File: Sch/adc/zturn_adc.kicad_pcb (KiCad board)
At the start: 4 copper layers, 90.5 x 80 mm, 117 parts, among them CN1 SMA, CN2 SMA, CN3 AudioJack, J1 JP4, J2 Header5, J3 JP2, J4 JP2, J5 JP2, J6 JP2, P1 CONN_02X40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

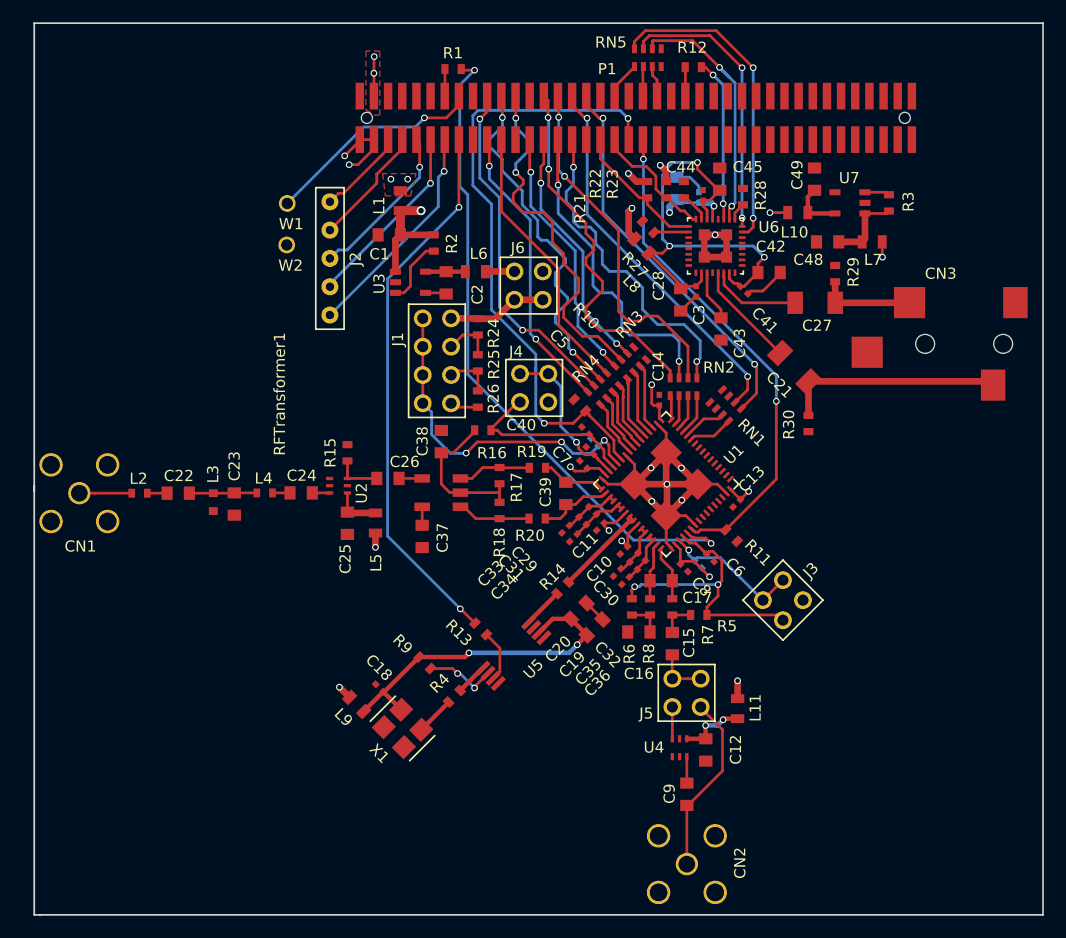
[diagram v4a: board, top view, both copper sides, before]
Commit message: moved jumper
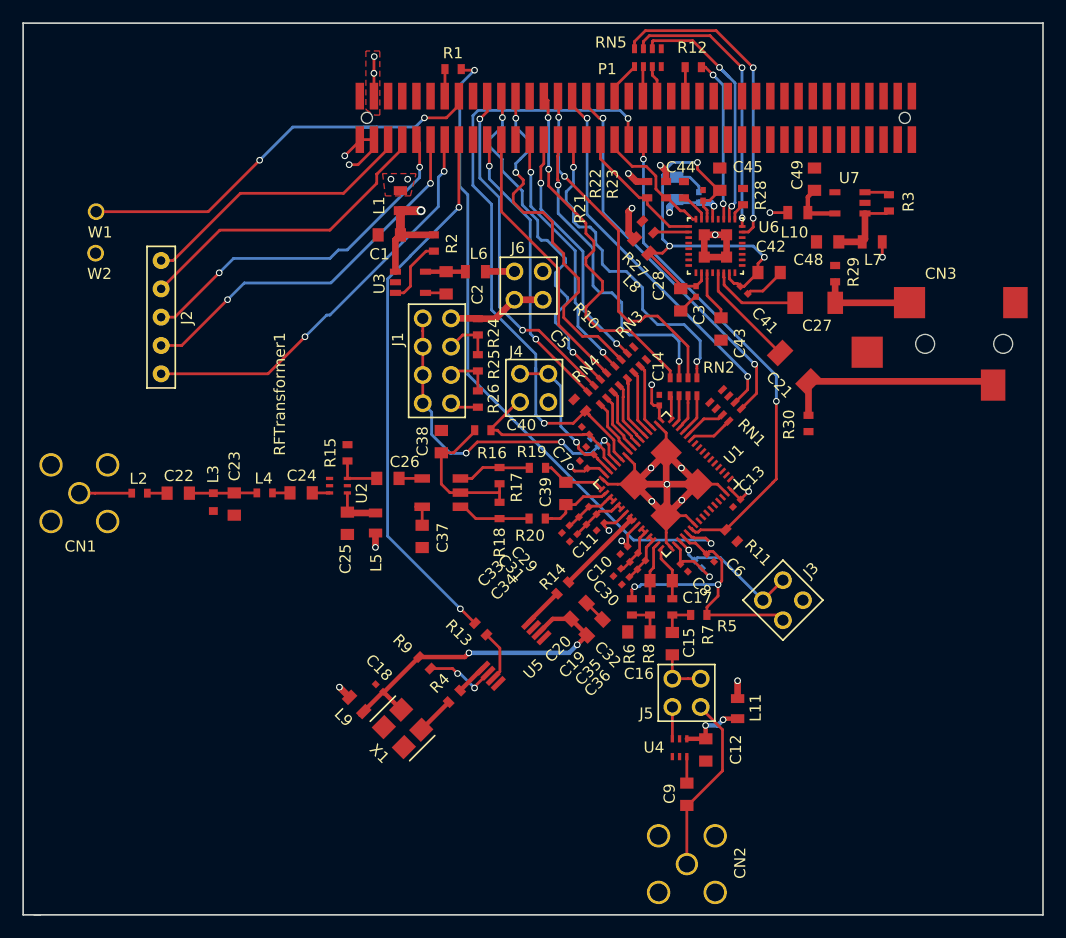
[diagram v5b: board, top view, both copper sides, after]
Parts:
- moved W1 17.2 mm to (92.5, 71.9)
- moved W2 17.2 mm to (92.5, 75.6)
- moved J2 16.0 mm to (98.4, 81.4)
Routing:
- net /CN/VDDIO_13_PL: track 20.7 -> 39.3 mm, vias 1 -> 2
- net /CN/JTAG_TMS: track 10.8 -> 28.1 mm
- net /CN/JTAG_TDI: track 14.6 -> 31.9 mm, vias 1 -> 2
- net /CN/JTAG_NRST: track 20.0 -> 37.3 mm, vias 1 -> 2
- net /CN/JTAG_TCK: track 8.01 -> 25.3 mm
- net /CN/JTAG_TDO: track 16.9 -> 34.1 mm, vias 1 -> 2
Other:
- board size 90.5 x 80 mm -> 91.5 x 80 mm
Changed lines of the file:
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@@
     (area 86.924999 47.3 188.35 135.075001)
     (thickness 1.6)
-    (drawings 8)
-    (tracks 970)
+    (drawings 7)
+    (tracks 991)
     (zones 0)
     (modules 117)
@@
   )
   (module adc_lib:M20-9990546 (layer F.Cu)
-    (at 113.525 76.11 270)
+    (at 98.38 81.38 270)
     (fp_text reference J2 (at 0.05 -2.305 270) (layer F.SilkS)
       (effects (font (size 1 1) (thickness 0.15)))
@@
   )
   (module adc_lib:68000-401HLF (layer F.Cu)
-    (at 109.7 71.175)
+    (at 92.55 71.915)
     (fp_text reference W1 (at 0.35 1.85) (layer F.SilkS)
       (effects (font (size 1 1) (thickness 0.15)))
@@
   )
   (module adc_lib:68000-401HLF (layer F.Cu)
-    (at 109.65 74.9)
+    (at 92.5 75.64)
     (fp_text reference W2 (at 0.35 1.85) (layer F.SilkS)
       (effects (font (size 1 1) (thickness 0.15)))
@@
     (arrow2b (pts (xy 180.5 55) (xy 181.086421 56.126504)))
   )
-  (dimension 89.5 (width 0.3) (layer Dwgs.User)
-    (gr_text "89.500 mm" (at 131.75 48.65) (layer Dwgs.User)
+  (dimension 91.440005 (width 0.3) (layer Dwgs.User)
+    (gr_text "91.440 mm" (at 131.741801 48.565 359.9812022) (layer Dwgs.User)
       (effects (font (size 1.5 1.5) (thickness 0.3)))
     )
-    (feature1 (pts (xy 176.5 54) (xy 176.5 47.3)))
-    (feature2 (pts (xy 87 54) (xy 87 47.3)))
-    (crossbar (pts (xy 87 50) (xy 176.5 50)))
-    (arrow1a (pts (xy 176.5 50) (xy 175.373496 50.586421)))
-    (arrow1b (pts (xy 176.5 50) (xy 175.373496 49.413579)))
-    (arrow2a (pts (xy 87 50) (xy 88.126504 50.586421)))
-    (arrow2b (pts (xy 87 50) (xy 88.126504 49.413579)))
+    (feature1 (pts (xy 177.46 54.07) (xy 177.462244 47.23)))
+    (feature2 (pts (xy 86.02 54.04) (xy 86.022244 47.2)))
+    (crossbar (pts (xy 86.021358 49.9) (xy 177.461358 49.93)))
+    (arrow1a (pts (xy 177.461358 49.93) (xy 176.334662 50.516051)))
+    (arrow1b (pts (xy 177.461358 49.93) (xy 176.335047 49.34321)))
+    (arrow2a (pts (xy 86.021358 49.9) (xy 87.147669 50.48679)))
+    (arrow2b (pts (xy 86.021358 49.9) (xy 87.148054 49.313949)))
   )
   (gr_line (start 87 135) (end 87.5 135) (layer Edge.Cuts) (width 0.15))
-  (gr_line (start 87 96.5) (end 87 135) (layer Edge.Cuts) (width 0.15))
-  (gr_line (start 177.5 135) (end 87.5 135) (layer Edge.Cuts) (width 0.15))
+  (gr_line (start 177.5 135) (end 86 135) (layer Edge.Cuts) (width 0.15))
   (gr_line (start 177.5 55) (end 177.5 135) (layer Edge.Cuts) (width 0.15))
-  (gr_line (start 87 55) (end 177.5 55) (layer Edge.Cuts) (width 0.15))
-  (gr_line (start 87 97) (end 87 55) (layer Edge.Cuts) (width 0.15))
+  (gr_line (start 86 55) (end 177.5 55) (layer Edge.Cuts) (width 0.15))
+  (gr_line (start 86 55) (end 86 135) (layer Edge.Cuts) (width 0.15))
   (segment (start 119.85 71.825) (end 119.85 74) (width 0.8) (layer F.Cu) (net 1))
   (segment (start 119.85 71.825) (end 121.7 71.825) (width 0.8) (layer F.Cu) (net 1))
@@
   (segment (start 126.797898 86.20742) (end 126.797899 86.207421) (width 0.25) (layer F.Cu) (net 40))
   (segment (start 126.797899 86.207421) (end 126.797899 87.997422) (width 0.25) (layer F.Cu) (net 40))
-  (segment (start 113.525 71.03) (end 114.286999 70.268001) (width 0.25) (layer F.Cu) (net 41))
-  (segment (start 114.286999 70.268001) (end 114.746999 70.268001) (width 0.25) (layer F.Cu) (net 41))
+  (segment (start 98.38 76.3) (end 99.45763 76.3) (width 0.25) (layer F.Cu) (net 41))
+  (segment (start 99.45763 76.3) (end 105.489629 70.268001) (width 0.25) (layer F.Cu) (net 41))
+  (segment (start 105.489629 70.268001) (end 114.746999 70.268001) (width 0.25) (layer F.Cu) (net 41))
   (segment (start 114.746999 70.268001) (end 118.745 66.27) (width 0.25) (layer F.Cu) (net 41))
   (segment (start 118.745 66.27) (end 118.745 65.45) (width 0.25) (layer F.Cu) (net 41))
+  (segment (start 98.38 78.84) (end 103.65 73.57) (width 0.25) (layer F.Cu) (net 42))
+  (segment (start 103.65 73.57) (end 113.525 73.57) (width 0.25) (layer F.Cu) (net 42))
   (segment (start 113.525 73.57) (end 117.725 69.37) (width 0.25) (layer F.Cu) (net 42))
   (segment (start 117.725 69.37) (end 117.725 68.55) (width 0.25) (layer F.Cu) (net 42))
@@
   (segment (start 117.735 68.55) (end 120.015 66.27) (width 0.25) (layer F.Cu) (net 42))
   (segment (start 120.015 66.27) (end 120.015 65.45) (width 0.25) (layer F.Cu) (net 42))
+  (segment (start 103.59 77.4) (end 104.88 76.11) (width 0.25) (layer B.Cu) (net 43))
+  (segment (start 104.88 76.11) (end 113.525 76.11) (width 0.25) (layer B.Cu) (net 43))
+  (segment (start 98.38 81.38) (end 99.61 81.38) (width 0.25) (layer F.Cu) (net 43))
+  (segment (start 99.61 81.38) (end 103.59 77.4) (width 0.25) (layer F.Cu) (net 43))
+  (via (at 103.59 77.4) (size 0.6) (drill 0.4) (layers F.Cu B.Cu) (net 43))
   (segment (start 121.575 67.925) (end 121.575 65.74) (width 0.25) (layer F.Cu) (net 43))
   (segment (start 121.575 65.74) (end 121.285 65.45) (width 0.25) (layer F.Cu) (net 43))
@@
   (segment (start 121.575 68.850002) (end 121.575 67.925) (width 0.25) (layer B.Cu) (net 43))
   (via (at 121.575 67.925) (size 0.6) (drill 0.4) (layers F.Cu B.Cu) (net 43))
-  (segment (start 122.55 69.375) (end 113.525 78.4) (width 0.25) (layer B.Cu) (net 44))
-  (segment (start 113.525 78.4) (end 113.525 78.65) (width 0.25) (layer B.Cu) (net 44))
+  (segment (start 122.55 69.375) (end 113.615 78.31) (width 0.25) (layer B.Cu) (net 44))
+  (segment (start 104.34 79.81) (end 105.84 78.31) (width 0.25) (layer B.Cu) (net 44))
+  (segment (start 105.84 78.31) (end 113.615 78.31) (width 0.25) (layer B.Cu) (net 44))
+  (segment (start 98.38 83.92) (end 100.23 83.92) (width 0.25) (layer F.Cu) (net 44))
+  (segment (start 100.23 83.92) (end 104.34 79.81) (width 0.25) (layer F.Cu) (net 44))
+  (via (at 104.34 79.81) (size 0.6) (drill 0.4) (layers F.Cu B.Cu) (net 44))
   (segment (start 122.555 65.45) (end 122.555 69.37) (width 0.25) (layer F.Cu) (net 44))
   (segment (start 122.555 69.37) (end 122.55 69.375) (width 0.25) (layer F.Cu) (net 44))
   (via (at 122.55 69.375) (size 0.6) (drill 0.4) (layers F.Cu B.Cu) (net 44))
+  (segment (start 111.29 83.14) (end 113.24 81.19) (width 0.25) (layer B.Cu) (net 45))
+  (segment (start 113.24 81.19) (end 113.525 81.19) (width 0.25) (layer B.Cu) (net 45))
+  (segment (start 98.38 86.46) (end 107.97 86.46) (width 0.25) (layer F.Cu) (net 45))
+  (segment (start 107.97 86.46) (end 111.29 83.14) (width 0.25) (layer F.Cu) (net 45))
+  (via (at 111.29 83.14) (size 0.6) (drill 0.4) (layers F.Cu B.Cu) (net 45))
   (segment (start 123.775 68.3) (end 123.775 65.5) (width 0.25) (layer F.Cu) (net 45))
   (segment (start 123.775 65.5) (end 123.825 65.45) (width 0.25) (layer F.Cu) (net 45))
@@
   (segment (start 123.845 61.53) (end 123.825 61.55) (width 0.25) (layer F.Cu) (net 54))
   (segment (start 123.825 61.55) (end 123.825 60.545) (width 0.25) (layer F.Cu) (net 54))
+  (segment (start 121.174999 64.325001) (end 117.75 64.325001) (width 0.25) (layer B.Cu) (net 55))
+  (segment (start 117.75 64.325001) (end 116.549999 64.325001) (width 0.25) (layer B.Cu) (net 55))
+  (segment (start 107.22 67.3) (end 110.194999 64.325001) (width 0.25) (layer B.Cu) (net 55))
+  (segment (start 110.194999 64.325001) (end 117.75 64.325001) (width 0.25) (layer B.Cu) (net 55))
+  (segment (start 92.55 71.915) (end 102.605 71.915) (width 0.25) (layer F.Cu) (net 55))
+  (segment (start 102.605 71.915) (end 107.22 67.3) (width 0.25) (layer F.Cu) (net 55))
+  (via (at 107.22 67.3) (size 0.6) (drill 0.4) (layers F.Cu B.Cu) (net 55))
   (segment (start 122 63.5) (end 121.174999 64.325001) (width 0.25) (layer B.Cu) (net 55))
-  (segment (start 121.174999 64.325001) (end 116.549999 64.325001) (width 0.25) (layer B.Cu) (net 55))
-  (segment (start 116.549999 64.325001) (end 110.449999 70.425001) (width 0.25) (layer B.Cu) (net 55))
-  (segment (start 110.449999 70.425001) (end 109.7 71.175) (width 0.25) (layer B.Cu) (net 55))
   (segment (start 125.095 61.55) (end 125.095 62.37) (width 0.25) (layer F.Cu) (net 55))
   (segment (start 123.965 63.5) (end 122 63.5) (width 0.25) (layer F.Cu) (net 55))

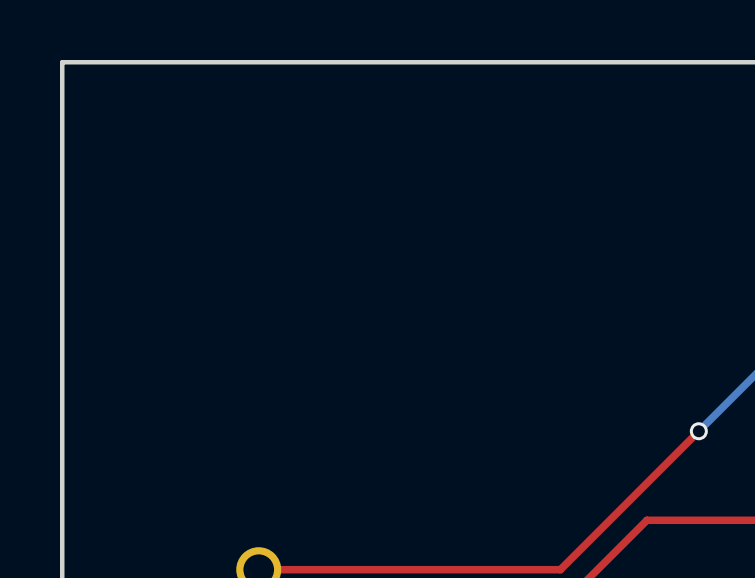
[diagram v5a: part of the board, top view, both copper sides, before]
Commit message: Add mounting hole
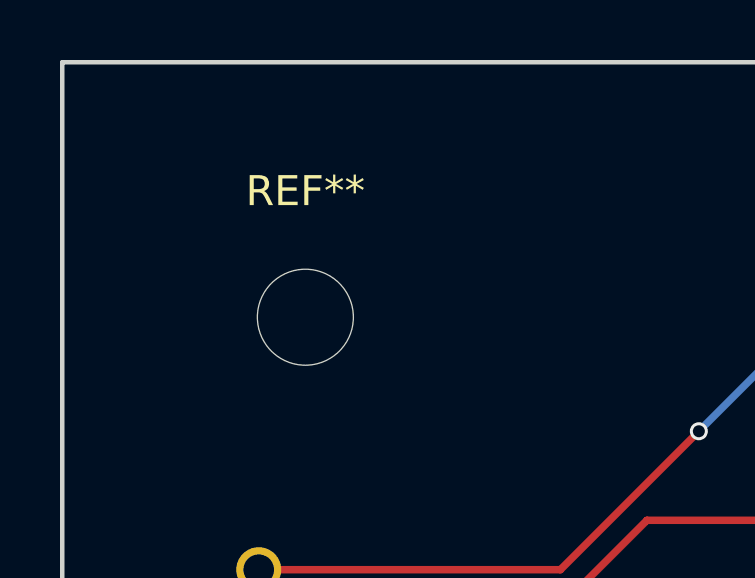
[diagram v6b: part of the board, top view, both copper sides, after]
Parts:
- added REF**: MountingHole_3.2mm_M3, Mounting_Holes:MountingHole_3.2mm_M3, F.Cu at (94.1, 63.5)
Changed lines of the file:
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@@
 (kicad_pcb (version 4) (host pcbnew 4.0.5)
   (general
-    (links 301)
+    (links 0)
     (no_connects 66)
-    (area 86.924999 47.3 188.35 135.075001)
+    (area 84.852381 47.2 188.35 135.075001)
     (thickness 1.6)
     (drawings 7)
     (tracks 991)
     (zones 0)
-    (modules 117)
+    (modules 118)
     (nets 189)
   )
@@
     (mod_text_size 1 1)
     (mod_text_width 0.15)
-    (pad_size 0.6 0.6)
-    (pad_drill 0.3)
+    (pad_size 3.2 3.2)
+    (pad_drill 3.2)
     (pad_to_mask_clearance 0.2)
     (aux_axis_origin 0 0)
@@
       (net 2 GND))
   )
+  (module Mounting_Holes:MountingHole_3.2mm_M3 (layer F.Cu)
+    (at 94.104 63.499)
+    (descr "Mounting Hole 3.2mm, no annular, M3")
+    (tags "mounting hole 3.2mm no annular m3")
+    (fp_text reference REF** (at 0 -4.2) (layer F.SilkS)
+      (effects (font (size 1 1) (thickness 0.15)))
+    )
+    (fp_text value MountingHole_3.2mm_M3 (at 0 4.2) (layer F.Fab)
+      (effects (font (size 1 1) (thickness 0.15)))
+    )
+    (fp_circle (center 0 0) (end 3.2 0) (layer Cmts.User) (width 0.15))
+    (fp_circle (center 0 0) (end 3.45 0) (layer F.CrtYd) (width 0.05))
+    (pad 1 np_thru_hole circle (at 0 0) (size 3.2 3.2) (drill 3.2) (layers *.Cu *.Mask))
+  )
   (dimension 80 (width 0.3) (layer Dwgs.User)

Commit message: Add pour GND
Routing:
- net (no net): track 0.00 -> 11.7 mm, vias 0 -> 1
- net GND: track 76.1 -> 70.1 mm, vias 8 -> 6
- added copper zone on B.Cu, net GND
- added copper zone on F.Cu, net GND
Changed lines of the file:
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@@
 (kicad_pcb (version 4) (host pcbnew 4.0.5)
   (general
-    (links 0)
-    (no_connects 66)
-    (area 84.852381 47.2 188.35 135.075001)
+    (links 301)
+    (no_connects 35)
+    (area 84.546857 47.2 188.35 135.075001)
     (thickness 1.6)
     (drawings 7)
-    (tracks 991)
+    (tracks 989)
     (zones 0)
     (modules 118)
@@
     (1 In1.Cu power hide)
     (2 In2.Cu power hide)
-    (31 B.Cu signal)
+    (31 B.Cu signal hide)
     (32 B.Adhes user)
     (33 F.Adhes user)
@@
     (last_trace_width 0.25)
     (trace_clearance 0.2)
-    (zone_clearance 0.2)
+    (zone_clearance 0.6)
     (zone_45_only no)
     (trace_min 0.2)
@@
   (gr_line (start 86 55) (end 177.5 55) (layer Edge.Cuts) (width 0.15))
   (gr_line (start 86 55) (end 86 135) (layer Edge.Cuts) (width 0.15))
+  (segment (start 117.37 79.23) (end 117.37 77.98141) (width 0.25) (layer B.Cu) (net 0))
+  (via (at 124.31 70.42) (size 0.6) (drill 0.4) (layers F.Cu B.Cu) (net 0))
+  (segment (start 117.37 77.98141) (end 124.31 71.04141) (width 0.25) (layer B.Cu) (net 0))
+  (segment (start 124.31 71.04141) (end 124.31 70.42) (width 0.25) (layer B.Cu) (net 0))
   (segment (start 119.85 71.825) (end 119.85 74) (width 0.8) (layer F.Cu) (net 1))
   (segment (start 119.85 71.825) (end 121.7 71.825) (width 0.8) (layer F.Cu) (net 1))
@@
   (segment (start 123.85 79.2) (end 123.95 79.3) (width 0.25) (layer F.Cu) (net 2))
   (segment (start 117.475 65.45) (end 117.475 66.27) (width 0.25) (layer F.Cu) (net 2))
-  (segment (start 117.475 66.27) (end 116.045 67.7) (width 0.25) (layer F.Cu) (net 2))
-  (segment (start 116.045 67.7) (end 115.25 67.7) (width 0.25) (layer F.Cu) (net 2))
-  (via (at 115.25 67.7) (size 0.6) (drill 0.4) (layers F.Cu B.Cu) (net 2))
   (segment (start 116.205 65.45) (end 116.205 65.553884) (width 0.25) (layer F.Cu) (net 2))
-  (segment (start 116.205 65.553884) (end 114.854442 66.904442) (width 0.25) (layer F.Cu) (net 2))
-  (via (at 114.854442 66.904442) (size 0.6) (drill 0.4) (layers F.Cu B.Cu) (net 2))
-  (segment (start 116.205 65.45) (end 117.475 65.45) (width 0.25) (layer F.Cu) (net 2))
   (segment (start 126.797898 89.457422) (end 124.745163 89.457421) (width 0.25) (layer F.Cu) (net 2))
   (segment (start 124.745163 89.457421) (end 124.394105 89.106362) (width 0.25) (layer F.Cu) (net 2))
@@
     (polygon
       (pts
-        (xy 118 55.5) (xy 87.5 55.5) (xy 87.5 134.5) (xy 176.930859 134.5) (xy 176.994082 55.5)
+        (xy 118 55.5) (xy 86.42 55.55) (xy 86.69 134.68) (xy 177.200859 134.63) (xy 176.994082 55.5)
       )
     )
   )
   (zone (net 48) (net_name +3V3) (layer F.Cu) (hatch edge 0.508)
+    (priority 2)
     (connect_pads yes (clearance 0.1))
     (min_thickness 0.254)
@@
   )
   (zone (net 48) (net_name +3V3) (layer F.Cu) (hatch full 0.508)
+    (priority 2)
     (connect_pads yes (clearance 0.1))
     (min_thickness 0.254)
@@
       )
     )
+  )
+  (zone (net 2) (net_name GND) (layer F.Cu) (hatch edge 0.508)
+    (connect_pads (clearance 0.6))
+    (min_thickness 0.254)
+    (fill yes (arc_segments 16) (thermal_gap 0.508) (thermal_bridge_width 0.508) (smoothing fillet))
+    (polygon
+      (pts
+        (xy 86.53 55.52) (xy 86.53 134.56) (xy 177.09 134.56) (xy 177.09 55.24) (xy 86.55 55.24)
+        (xy 86.51 55.2)
+      )
+    )
+    (polygon
+      (pts        (xy 124.93 78.34) (xy 124.83 80.49) (xy 126.34 80.87) (xy 128.43 80.81) (xy 129.58 78.78)
+        (xy 129.78 78.07) (xy 128.36 77.8) (xy 127.48 78.18) (xy 125.94 78.11)
+      )
+    )
+    (polygon
+      (pts        (xy 125.97 109.58) (xy 125.38 110.1) (xy 125.01 111.19) (xy 126.06 110.86) (xy 126.68 111.19)
+        (xy 126.81 112.01) (xy 127.37 111.88) (xy 127.98 111.76) (xy 128.27 111.19) (xy 127.72 110.82)
+        (xy 126.29 109.66)
+      )
+    )
+  )
+  (zone (net 2) (net_name GND) (layer B.Cu) (hatch edge 0.508)
+    (connect_pads (clearance 0.6))
+    (min_thickness 0.254)
+    (fill yes (arc_segments 16) (thermal_gap 0.508) (thermal_bridge_width 0.508) (smoothing fillet) (radius 0.02))
+    (polygon
+      (pts
+        (xy 86.3 55.38) (xy 86.3 134.71) (xy 177.21 134.68) (xy 177.21 55.43) (xy 177.21 55.11)
+        (xy 86.31 55.11) (xy 86.3 55.1)
+      )
+    )
